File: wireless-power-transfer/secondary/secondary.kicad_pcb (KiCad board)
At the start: 2 copper layers, 100 x 58 mm, 10 parts, among them J1 Screw_Terminal_1x02, J2 Screw_Terminal_1x02, U1 LM7812CT

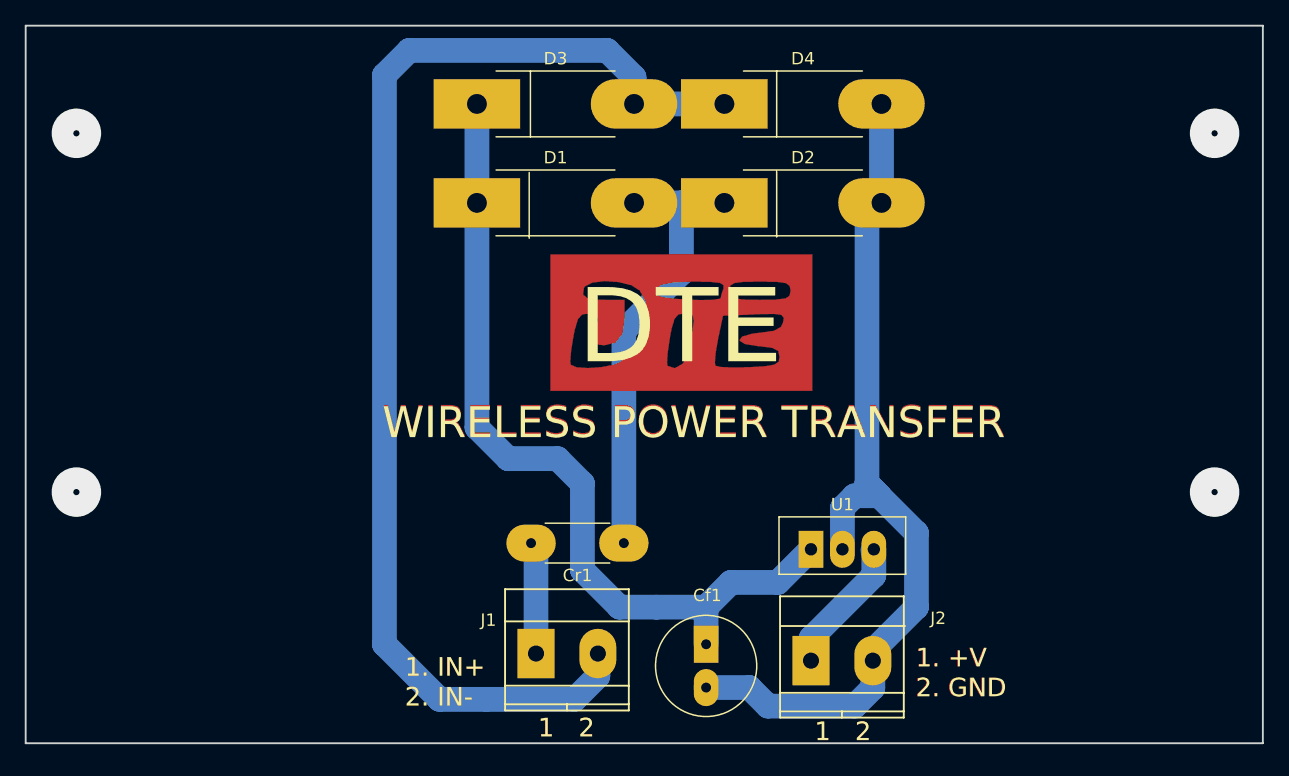
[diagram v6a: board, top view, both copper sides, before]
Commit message: Fix some errors in the border of boards to panelize them correctly
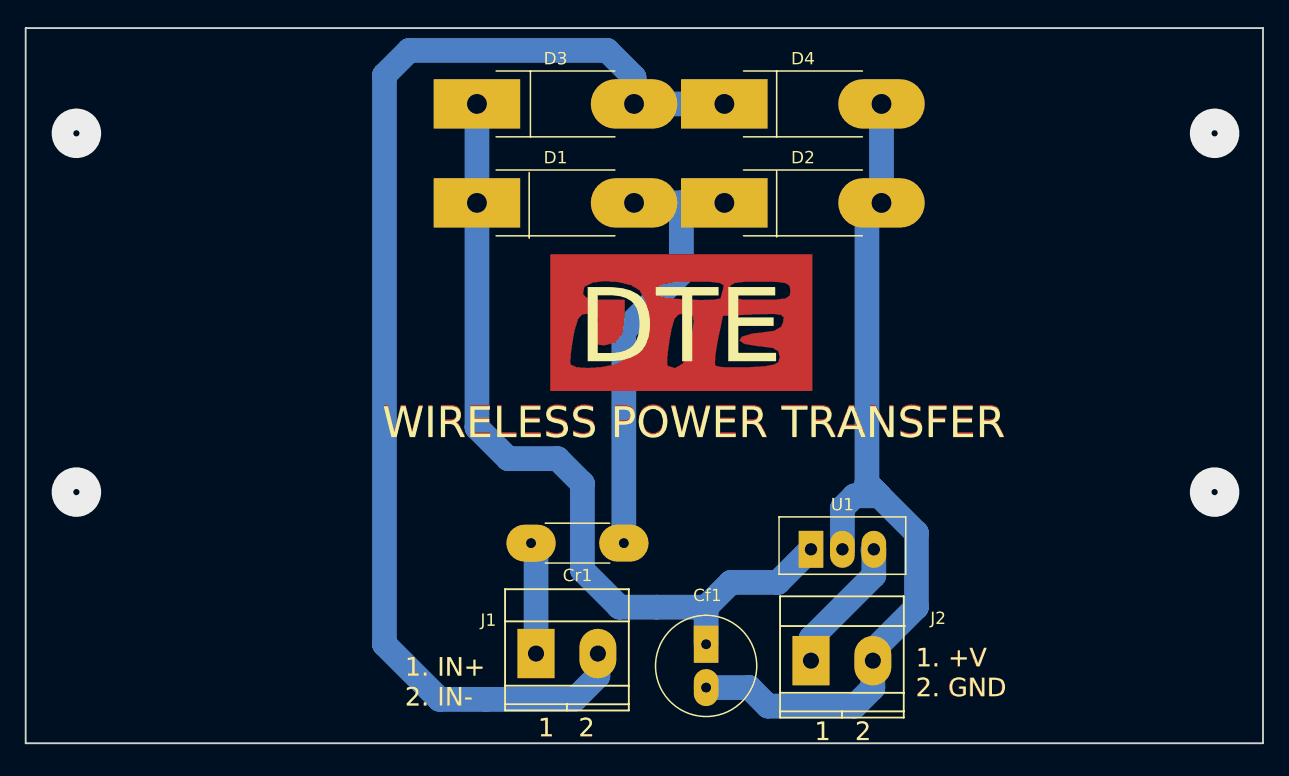
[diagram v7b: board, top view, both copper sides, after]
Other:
- board size 100 x 58 mm -> 100 x 57.8 mm
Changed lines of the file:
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@@
     (43 Eco2.User user hide)
     (44 Edge.Cuts user)
-    (45 Margin user hide)
+    (45 Margin user)
     (46 B.CrtYd user hide)
     (47 F.CrtYd user hide)
@@
     (pad_drill 1.3)
     (pad_to_mask_clearance 0.1)
-    (aux_axis_origin 0 0)
+    (aux_axis_origin 83.925 115.075)
     (visible_elements 7FFEFF69)
     (pcbplotparams
@@
       (xy 10.583333 5.521739)) (layer F.Cu) (width 0.01))
   )
+  (gr_line (start 84 115) (end 84 57.2) (angle 90) (layer Edge.Cuts) (width 0.15))
+  (gr_line (start 184.01 115) (end 184.01 57.2) (angle 90) (layer Edge.Cuts) (width 0.15))
   (gr_text "1   2" (at 127.7 113.75) (layer F.SilkS)
     (effects (font (size 1.5 1.5) (thickness 0.3)))
@@
     (effects (font (size 2.5 2.5) (thickness 0.5)))
   )
-  (gr_line (start 84 115) (end 84 57) (angle 90) (layer Edge.Cuts) (width 0.15))
   (gr_line (start 184 115) (end 84 115) (angle 90) (layer Edge.Cuts) (width 0.15))
-  (gr_line (start 184 57) (end 184 115) (angle 90) (layer Edge.Cuts) (width 0.15))
-  (gr_line (start 84 57) (end 184 57) (angle 90) (layer Edge.Cuts) (width 0.15))
+  (gr_line (start 84 57.195) (end 184 57.195) (angle 90) (layer Edge.Cuts) (width 0.15))
   (gr_text "WIRELESS POWER TRANSFER" (at 138 89) (layer F.Cu)
     (effects (font (size 2.5 2.5) (thickness 0.5)))

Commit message: PDFs created with schematics and PCB layers for front and back sides.
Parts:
- moved Cr1 36.9 mm to (105.8, 124.5)
- moved D1 36.9 mm to (94.0, 97.0)
- moved D2 36.9 mm to (114.0, 97.0)
- moved D3 36.9 mm to (94.0, 89.0)
- moved D4 36.9 mm to (114.0, 89.0)
- moved G*** 36.9 mm to (110.5, 106.7)
- moved J2 36.9 mm to (121.0, 134.0)
- moved U1 36.9 mm to (121.0, 125.0)
- moved Cf1 36.9 mm to (112.5, 132.7)
- moved J1 36.9 mm to (98.8, 133.4)
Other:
- board text added: "6/7"
- board text removed: "DTE"
